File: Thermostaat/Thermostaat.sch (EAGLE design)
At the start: 30 parts, among them IC2 MEGA8-P

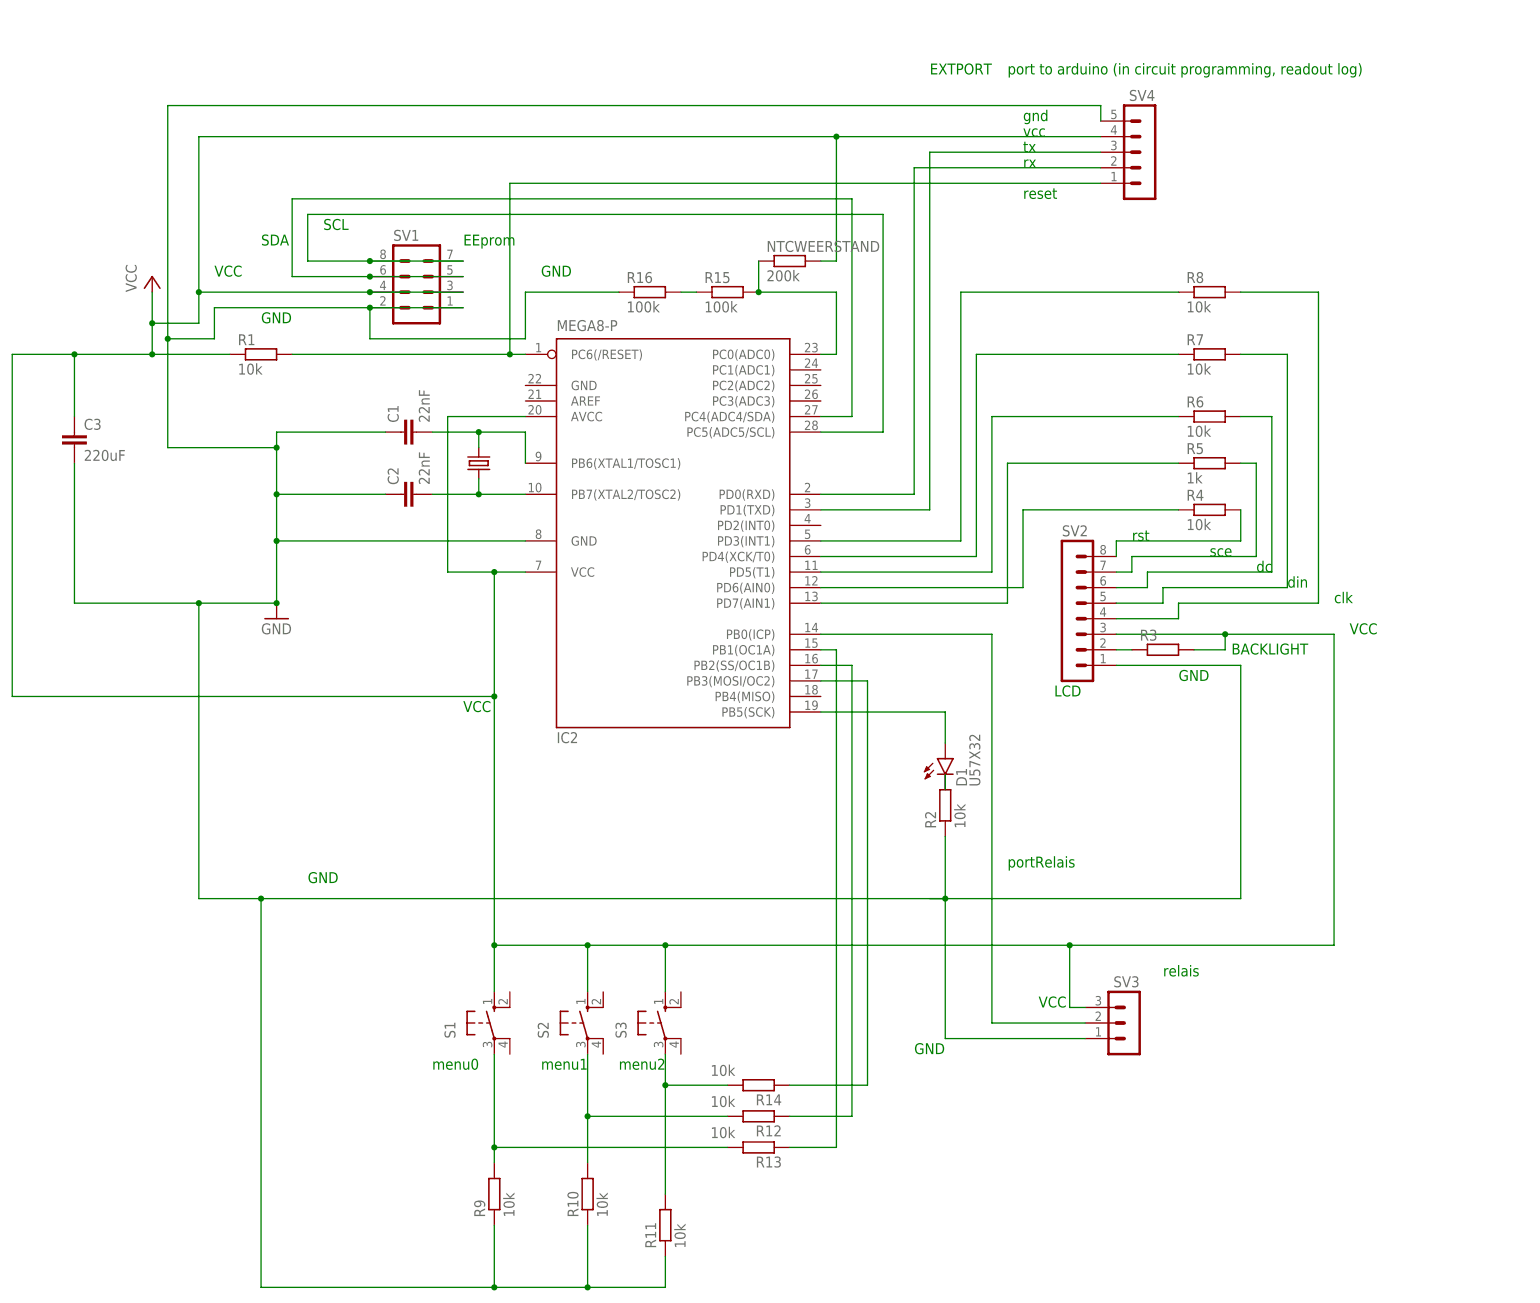
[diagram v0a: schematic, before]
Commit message: transistor toegevoegd voor relais
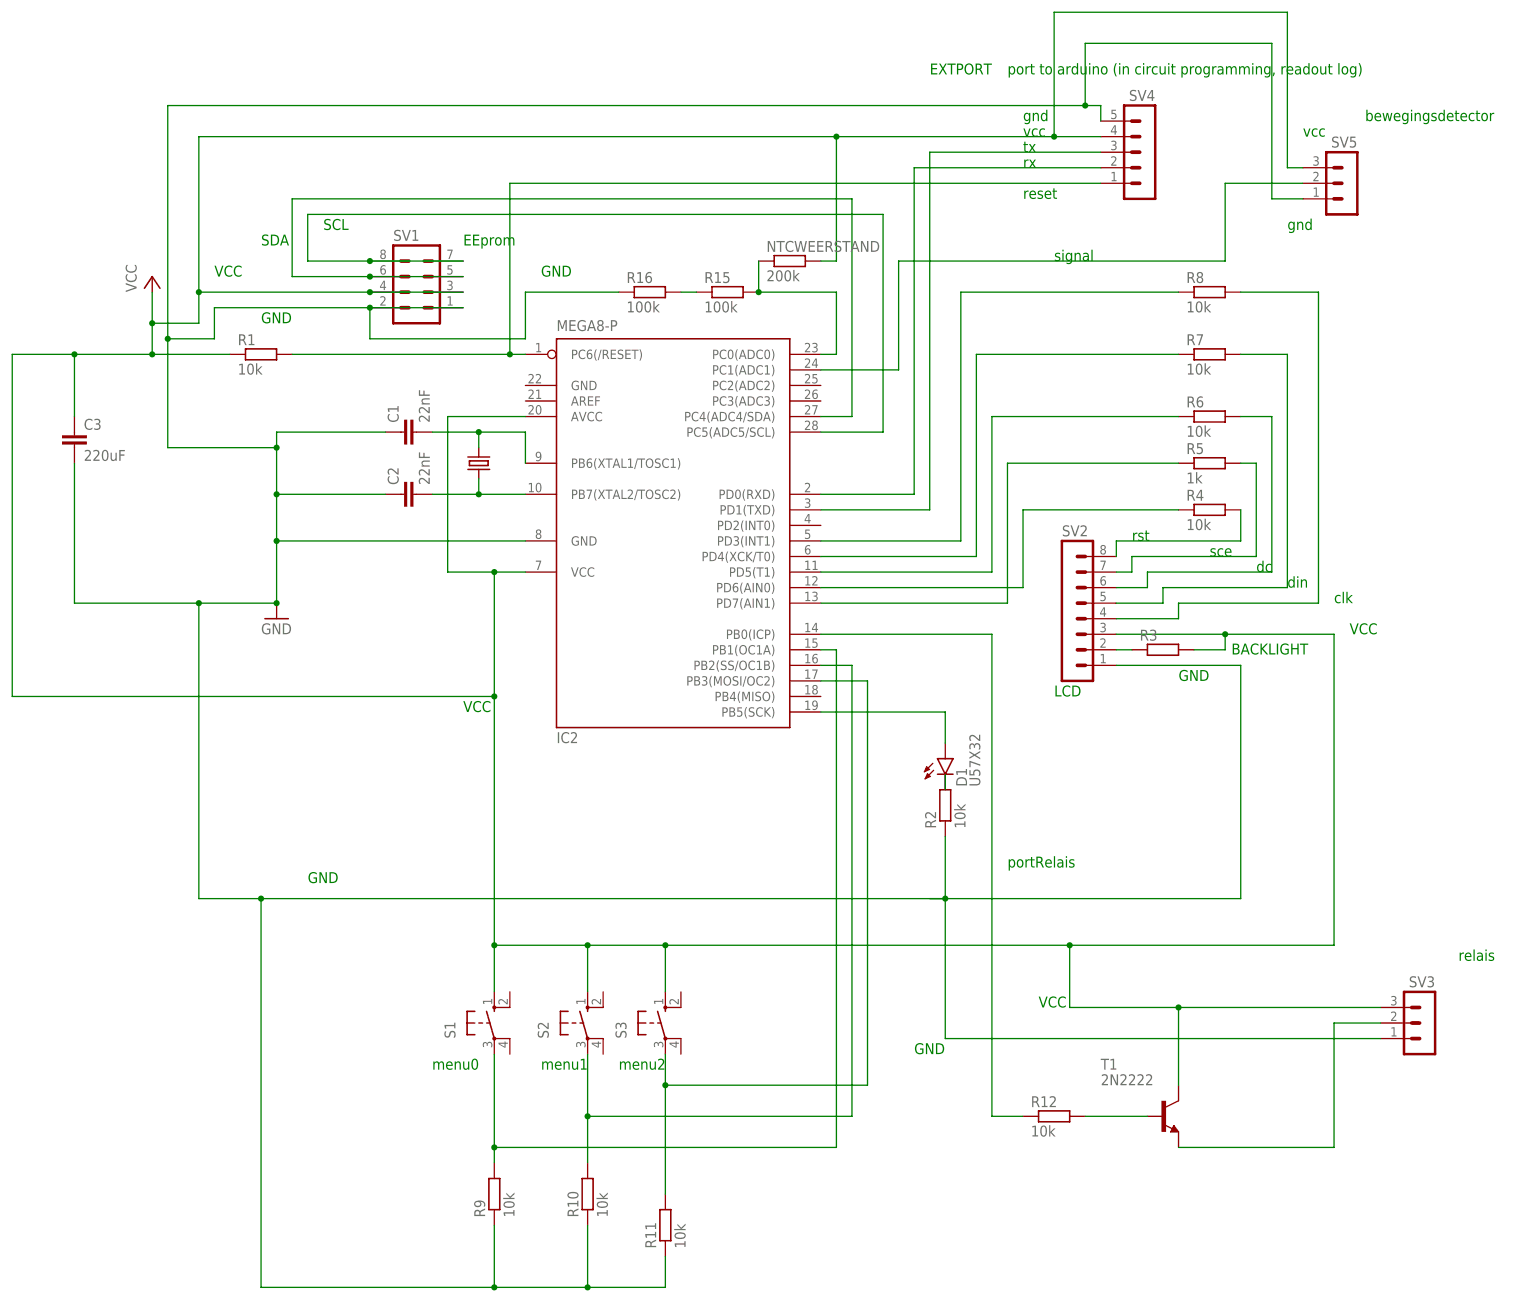
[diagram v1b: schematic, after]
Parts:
- removed R13, R14: 10k, rcl:R-EU_0204/7
- added SV5: (no value), con-lstb:MA03-1
- added T1: 2N2222, transistor:2N2222
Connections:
- removed net N$21: IC2.PB3(MOSI/OC2), R14.1
- new net N$5: IC2.PC1(ADC1), SV5.2
- net GND: now also SV5.1
- net N$18: now also SV3.2, T1.E; no longer IC2.PB2(SS/OC1B), R12.1
- net N$19: now also R12.2, T1.B; no longer IC2.PB1(OC1A), R13.1
- net N$20: now also R12.1; no longer SV3.2
- net N$25: now also IC2.PB3(MOSI/OC2); no longer R14.2
- net N$26: now also IC2.PB2(SS/OC1B); no longer R12.2
- net N$27: now also IC2.PB1(OC1A); no longer R13.2
- net VCC: now also SV5.3, T1.C
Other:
- note added: "bewegingsdetector"
- note added: "signal"
- moved on the sheet: R12, SV3
